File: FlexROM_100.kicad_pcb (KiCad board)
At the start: 2 copper layers, 16.5 x 34.3 mm, 7 parts, among them J1 LH535618 DIP LEGS, U1 28C256

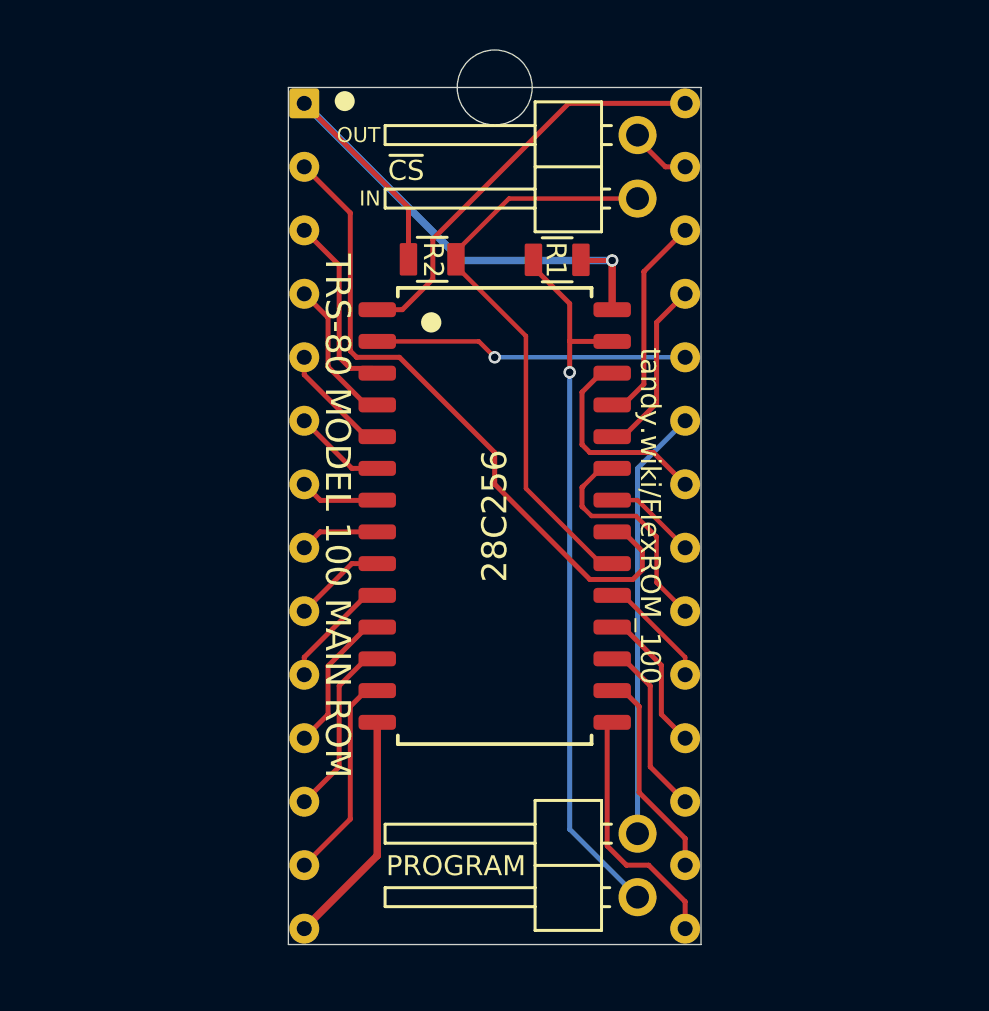
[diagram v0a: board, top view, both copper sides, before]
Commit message: add DS1000_DIP14
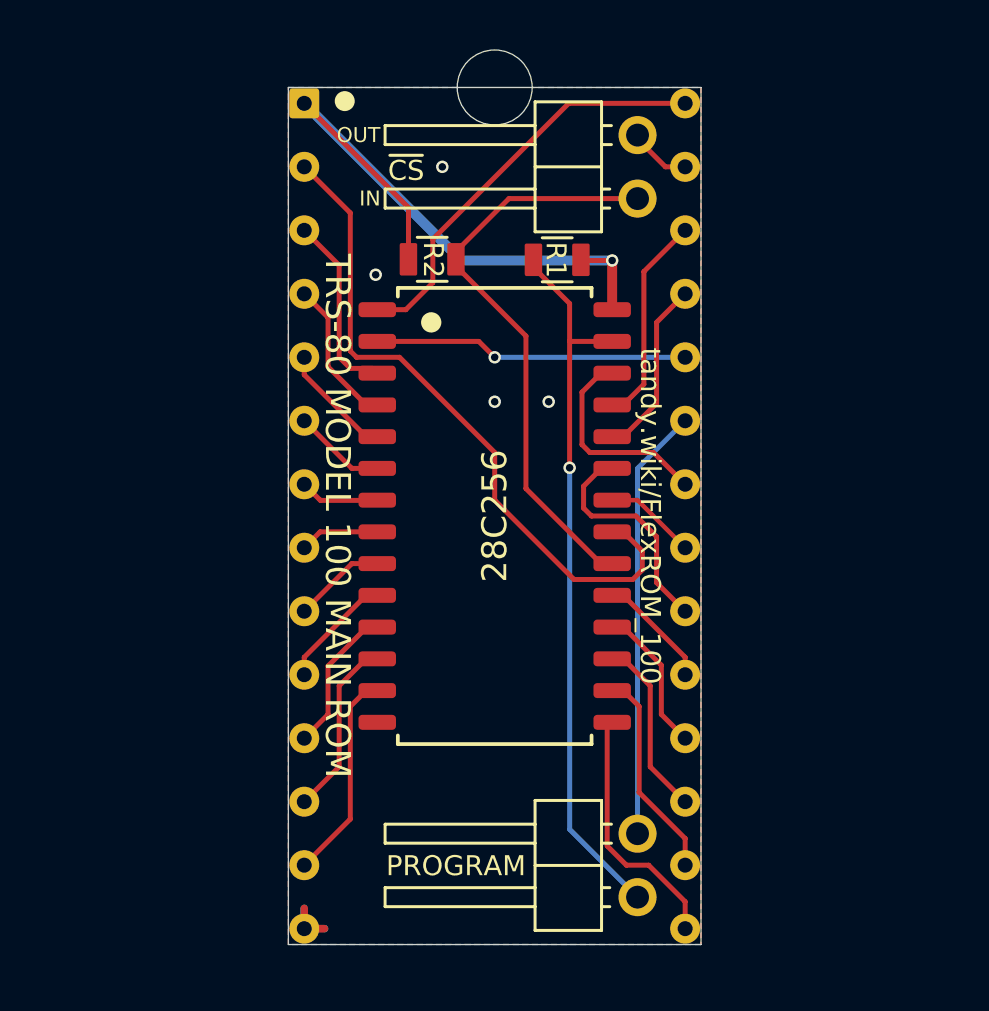
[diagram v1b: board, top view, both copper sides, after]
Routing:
- net /GND: track 9.46 -> 3.25 mm, vias 0 -> 4
- added copper zone on B.Cu, net /GND
- added copper zone on F.Cu, net /GND
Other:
- net class Default: clearance 0.16 -> 0.2; trace_width 0.18 -> 0.2
- rule trace_clearance: 0.16 -> 0.2
- rule trace_min: 0.16 -> 0.2

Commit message: kicad 6
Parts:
- JP1: value ~CS~ breakout -> ~{CS} breakout
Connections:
- net /~CS_IN renamed /~{CS_IN}
- net /~CS_OUT renamed /~{CS_OUT}
- net /~OE renamed /~{OE}
- net /~WE renamed /~{WE}
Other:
- net class Default removed
- board text added: "Connect ~{CS} OUT to REX TP1. Leave ~{CS} IN unconnected."
- board text added: "If REX is later removed, connect ~{CS} OUT to ~{CS} IN."
- board text added: "Install a shunt on ~{CS}, or, install wires as above,"
- board text added: "Run 2 wires from ~{CS} IN & ~{CS} OUT to Option ROM compartment."
- board text added: "~{CS}"
- board text removed: "Connect ~CS~ OUT to REX TP1. Leave ~CS~ IN unconnected."
- board text removed: "If REX is later removed, connect ~CS~ OUT to ~CS~ IN."
- board text removed: "Install a shunt on ~CS~, or, install wires as above,"
- board text removed: "Run 2 wires from ~CS~ IN & ~CS~ OUT to Option ROM compartment."
- board text removed: "~CS"

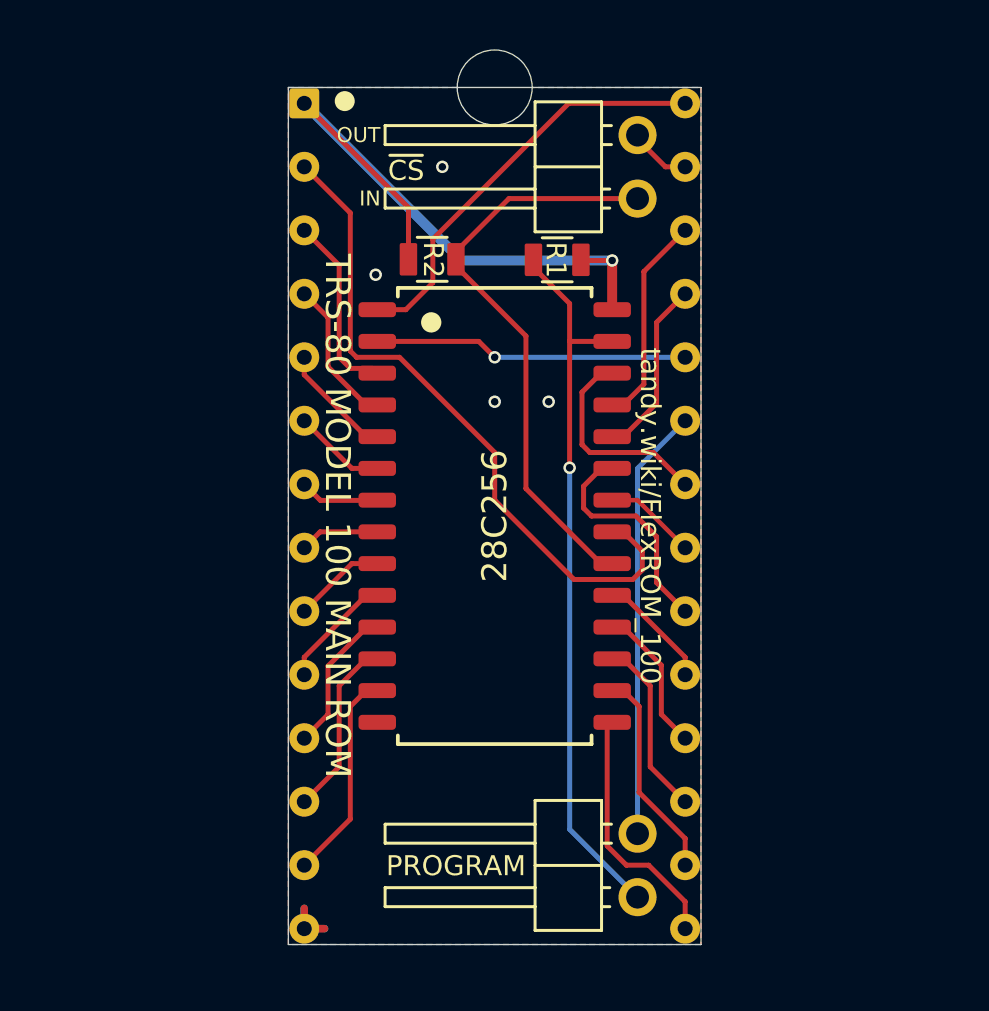
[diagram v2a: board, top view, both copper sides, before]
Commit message: programming adapter board outline & ground pour
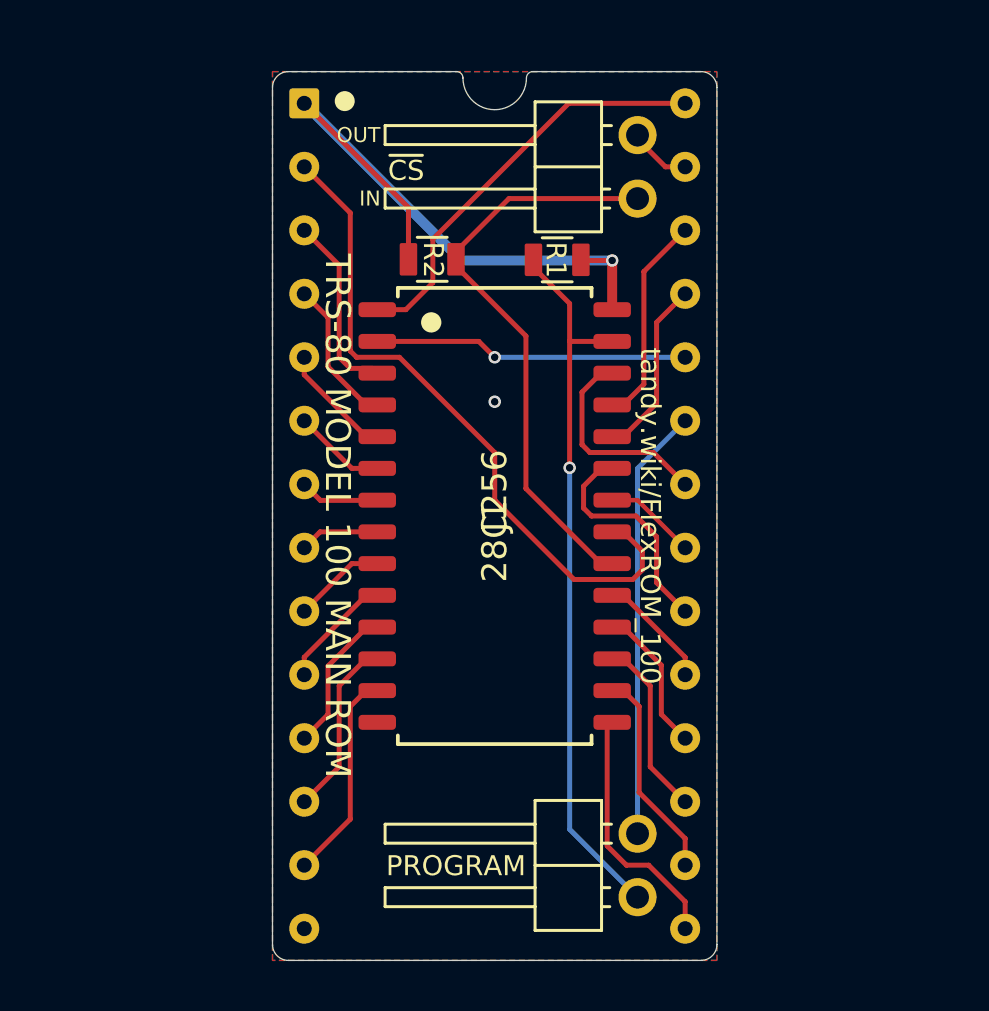
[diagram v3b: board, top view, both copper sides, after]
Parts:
- removed REF**: NPTH_3mm, 000_LOCAL:NPTH_3mm
- J1: footprint 000_LOCAL:DIP28_0.6_pcb_sil_pins -> 000_LOCAL:DIP28_0.6_pcb
- JP1: value ~{CS} breakout -> ~CS~ breakout
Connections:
- net /GND renamed GND
- net /VCC renamed VCC
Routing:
- net GND: track 3.25 -> 0.00 mm, vias 4 -> 1
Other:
- board size 16.5 x 34.3 mm -> 17.8 x 35.6 mm

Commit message: various minor cleanups
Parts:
- moved JP2 23.0 mm to (165.2, 94.3), turned to -90 degrees
- moved JP1 19.7 mm to (137.3, 94.3), turned to -90 degrees
- moved R2 14.9 mm to (139.7, 102.5), turned to -90 degrees
- moved R1 14.9 mm to (139.8, 97.5), turned to -90 degrees
- turned J1 to 90 degrees
- turned U1 to 90 degrees
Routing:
- net GND: vias 1 -> 0
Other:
- board size 17.8 x 35.6 mm -> 35.6 x 17.8 mm
- board text added: "${TITLE} ${REVISION} ${COMMENT2}"
- board text added: "R1: ${00000000-0000-0000-0000-00005fbb7cd5:VALUE} Legs: TE 1544210"
- board text added: "REX_Classic main ROM support: ~{CS}_OUT to REX TP1 to boot REX main rom ~{CS}_OUT to ~{CS}_IN to boot internal main rom"
- board text removed: "Connect ~{CS} OUT to REX TP1. Leave ~{CS} IN unconnected."
- board text removed: "If REX is later removed, connect ~{CS} OUT to ~{CS} IN."
- board text removed: "Install a shunt on ~{CS}, or, install wires as above,"
- board text removed: "Legs: TE 1544210"
- board text removed: "R1, R2: 47k"
- board text removed: "REX can then be added later without disassembling."
- board text removed: "Run 2 wires from ~{CS} IN & ~{CS} OUT to Option ROM compartment."
- board text removed: "To use REX Main ROM feature:"
- board text removed: "To use without REX:"
- board text removed: "and connect them to each other in the Option ROM compartment."

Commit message: minor touches
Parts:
- JP1: value ~CS~ breakout -> ~{CS} breakout
- JP2: value PROGRAM -> PROGRAM/RUN
- R1, R2: value 47K -> 100K
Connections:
- net /~{CS_IN} renamed /~{CS_IC}
- net /~{CS_OUT} renamed /~{CS_BUS}
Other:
- board text added: "BUS"
- board text added: "IC"
- board text added: "REX_Classic main ROM support: ~{CS}_BUS to REX TP1 to boot REX main rom ~{CS}_BUS to ~{CS}_IC to boot internal main rom"
- board text removed: "IN"
- board text removed: "OUT"
- board text removed: "REX_Classic main ROM support: ~{CS}_OUT to REX TP1 to boot REX main rom ~{CS}_OUT to ~{CS}_IN to boot internal main rom"
